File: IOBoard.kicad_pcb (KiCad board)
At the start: 2 copper layers, 53 x 33 mm, 11 parts, among them J1 EXP1, J2 EXP2, J3 LCD_EXP1, J4 LCD_EXP2, J5 EXP3, J6 EXP4

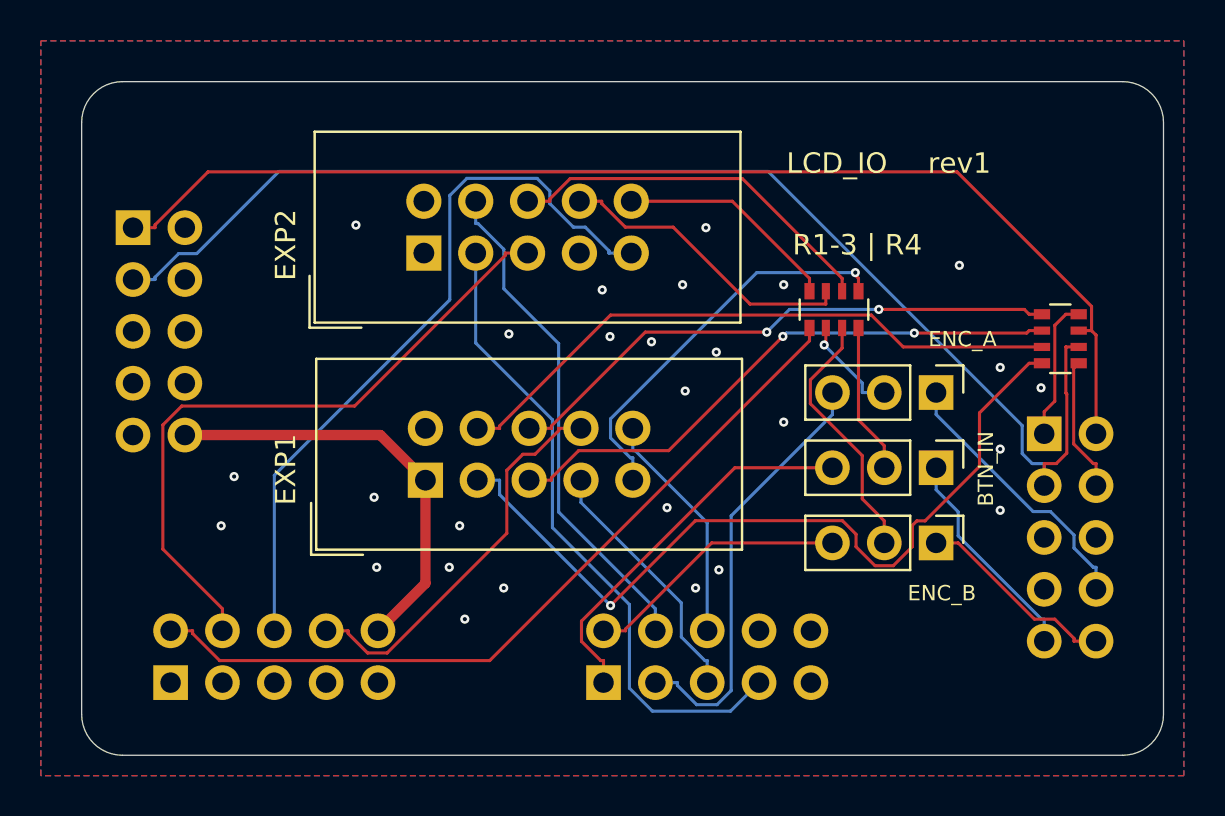
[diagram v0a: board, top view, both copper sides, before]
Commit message: Avoid using 3.3V only pins for IO board.
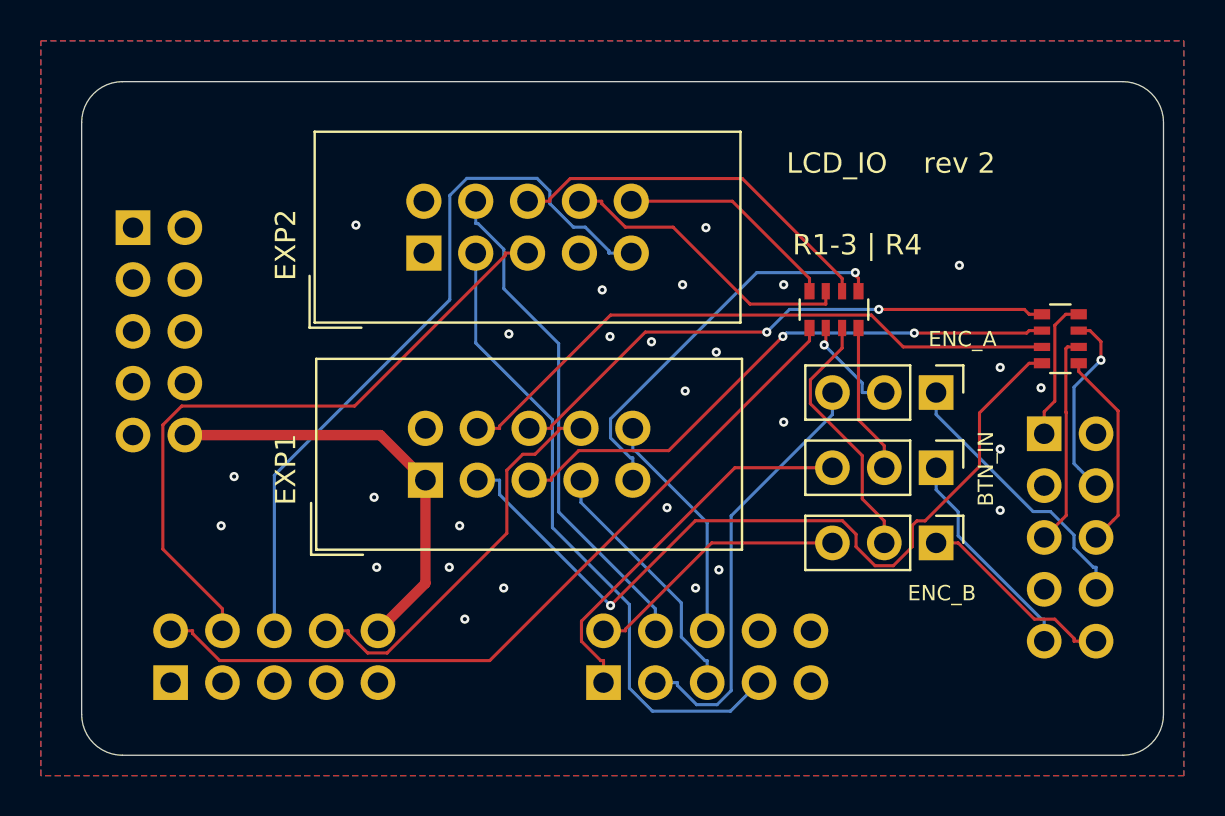
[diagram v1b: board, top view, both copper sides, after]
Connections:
- J2 pad 2: /IOA_4 -> (no net)
- J2 pad 3: /IOA_5 -> (no net)
- J2 pad 5: (no net) -> /IOA_7
- J2 pad 6: (no net) -> /IOA_8
- J6 pad 1: /IOA_4 -> (no net)
- J6 pad 3: /IOA_5 -> (no net)
- RN2 pad 5: /IOA_6 -> /IOA_8
- RN2 pad 6: /IOA_5 -> /IOA_7
- RN2 pad 7: /IOA_4 -> /IOA_6
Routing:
- net /IOA_5: track 63.0 -> 0.00 mm
- net /IOA_4: track 57.9 -> 0.00 mm
- net /IOA_7: track 0.00 -> 10.4 mm
- net /IOA_8: track 0.00 -> 9.78 mm
- net /IOA_6: track 6.63 -> 9.36 mm, vias 0 -> 1
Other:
- board text added: "rev 2"
- board text removed: "rev1"

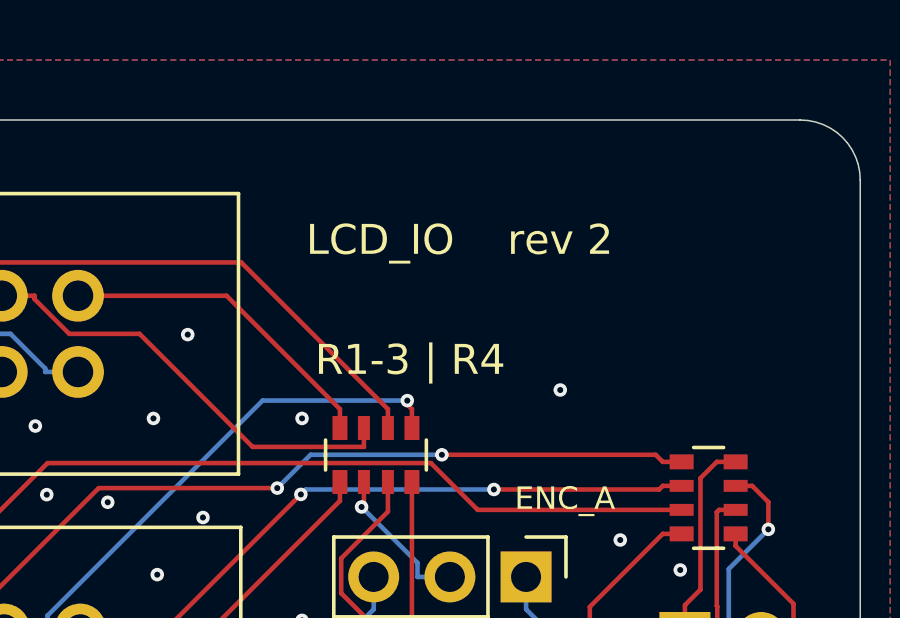
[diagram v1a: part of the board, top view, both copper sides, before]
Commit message: Add reverse power protection to the nucleo board.
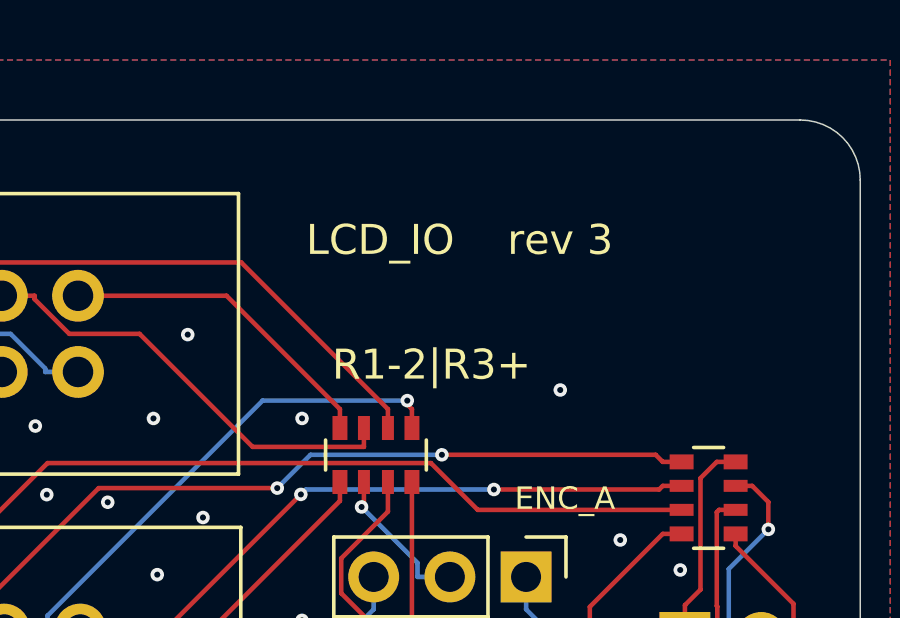
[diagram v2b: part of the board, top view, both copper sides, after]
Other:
- board text added: "(c) iQury.us Sept 2019"
- board text added: "R1-2|R3+"
- board text added: "rev 3"
- board text removed: "(c) iQury.us Aug 2019"
- board text removed: "R1-3 | R4"
- board text removed: "rev 2"

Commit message: New reveision of the IO board, correct LCD_EN signal.
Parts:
- added JP4: JP_LCD_EN, Connector_PinHeader_2.54mm:PinHeader_1x03_P2.54mm_Vertical, F.Cu at (103.9, 93.6)
- moved RN1 16.5 mm to (103.0, 109.2)
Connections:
- J2 pad 7: (no net) -> /IOA_15
- J3 pad 8: /~LCD_CS -> /LCD_EN
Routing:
- net /~LCD_CS: track 19.4 -> 51.2 mm
- net /LCD_D7: track 39.9 -> 64.1 mm, vias 1 -> 0
- net /IOA_15: track 0.00 -> 18.1 mm
- net /LCD_EN: track 0.00 -> 17.2 mm
- net /ENC_EN1: track 14.9 -> 31.0 mm, vias 0 -> 1
- net /MISO_IN: track 10.9 -> 26.8 mm, vias 0 -> 1
- net /ENC_EN2: track 18.6 -> 32.3 mm, vias 0 -> 1
- net Net-(JP3-Pad2): track 5.05 -> 16.4 mm
- net Net-(JP2-Pad2): track 12.7 -> 7.70 mm
- net /SPI2_SCK: track 36.1 -> 31.1 mm
- net Net-(JP1-Pad2): track 7.37 -> 11.2 mm
- net /LCD_D6: track 30.7 -> 33.8 mm
- net /IOE_4: track 12.5 -> 14.9 mm
- net /IOE_0: track 18.9 -> 16.7 mm
- net /IOE_6: track 31.8 -> 33.4 mm
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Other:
- board text added: "LCD_EN"
- board text added: "rev 4"
- board text removed: "rev 3"
